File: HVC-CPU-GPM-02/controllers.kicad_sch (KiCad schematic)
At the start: 31 parts, among them P2 EXPANSION, P4 CONTROLLER 1, P5 CONTROLLER 2, U7 74LS368, U8 74LS368

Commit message: annotate schematics, correct PCB/schematic parity issure, add datasheets
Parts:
- C11, C12, C13, C14, C15, C16, C17, C18, C19, C20, C21, C22, C23, C24, C25, C26, C27, C28, C29, C30, C31, C32, C33, C9: footprint Nintendo:C_Disc_D3.0mm_W2.0mm_P3.0mm -> Nintendo:C_Disc_NoSilk_D3.0mm_W2.0mm_P3.0mm
- R8: footprint Resistor_THT:R_Axial_DIN0207_L6.3mm_D2.5mm_P10.16mm_Horizontal -> Nintendo:R_Axial_NoSilk_DIN0207_L6.3mm_D2.5mm_P10.16mm_Horizontal
- RM1: footprint Resistor_THT:R_Array_SIP12 -> Nintendo:R_Array_SIP12
- U7, U8: footprint Package_DIP:DIP-16_W7.62mm -> Nintendo:DIP-16_W7.62mm
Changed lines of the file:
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@@
 			)
 		)
-		(property "Footprint" "Nintendo:C_Disc_D3.0mm_W2.0mm_P3.0mm"
+		(property "Footprint" "Nintendo:C_Disc_NoSilk_D3.0mm_W2.0mm_P3.0mm"
 			(at 77.7748 90.17 0)
 			(effects
@@
 			)
 		)
-		(property "Footprint" "Nintendo:C_Disc_D3.0mm_W2.0mm_P3.0mm"
+		(property "Footprint" "Nintendo:C_Disc_NoSilk_D3.0mm_W2.0mm_P3.0mm"
 			(at 82.8548 46.99 0)
 			(effects
@@
 			)
 		)
-		(property "Footprint" "Nintendo:C_Disc_D3.0mm_W2.0mm_P3.0mm"
+		(property "Footprint" "Nintendo:C_Disc_NoSilk_D3.0mm_W2.0mm_P3.0mm"
 			(at 101.2952 153.67 0)
 			(effects
@@
 			)
 		)
-		(property "Footprint" "Resistor_THT:R_Array_SIP12"
+		(property "Footprint" "Nintendo:R_Array_SIP12"
 			(at 141.478 99.06 90)
 			(effects
@@
 			)
 		)
-		(property "Footprint" "Nintendo:C_Disc_D3.0mm_W2.0mm_P3.0mm"
+		(property "Footprint" "Nintendo:C_Disc_NoSilk_D3.0mm_W2.0mm_P3.0mm"
 			(at 82.8548 90.17 0)
 			(effects
@@
 			)
 		)
-		(property "Footprint" "Resistor_THT:R_Array_SIP12"
+		(property "Footprint" "Nintendo:R_Array_SIP12"
 			(at 182.118 99.06 90)
 			(effects
@@
 			)
 		)
-		(property "Footprint" "Nintendo:C_Disc_D3.0mm_W2.0mm_P3.0mm"
+		(property "Footprint" "Nintendo:C_Disc_NoSilk_D3.0mm_W2.0mm_P3.0mm"
 			(at 91.1352 153.67 0)
 			(effects
@@
 			)
 		)
-		(property "Footprint" "Package_DIP:DIP-16_W7.62mm"
+		(property "Footprint" "Nintendo:DIP-16_W7.62mm"
 			(at 227.33 147.32 0)
 			(effects
@@
 			)
 		)
-		(property "Datasheet" "http://www.ti.com/lit/gpn/sn74LS368"
+		(property "Datasheet" "kicad-embed://74LS368.pdf"
 			(at 227.33 147.32 0)
 			(effects
@@
 			)
 		)
-		(property "Footprint" "Nintendo:C_Disc_D3.0mm_W2.0mm_P3.0mm"
+		(property "Footprint" "Nintendo:C_Disc_NoSilk_D3.0mm_W2.0mm_P3.0mm"
 			(at 70.8152 153.67 0)
 			(effects
@@
 			)
 		)
-		(property "Footprint" "Resistor_THT:R_Array_SIP12"
+		(property "Footprint" "Nintendo:R_Array_SIP12"
 			(at 168.148 26.67 90)
 			(effects
@@
 			)
 		)
-		(property "Footprint" "Resistor_THT:R_Array_SIP12"
+		(property "Footprint" "Nintendo:R_Array_SIP12"
 			(at 182.372 26.67 90)
 			(effects
@@
 			)
 		)
-		(property "Footprint" "Nintendo:C_Disc_D3.0mm_W2.0mm_P3.0mm"
+		(property "Footprint" "Nintendo:C_Disc_NoSilk_D3.0mm_W2.0mm_P3.0mm"
 			(at 191.4652 63.5 0)
 			(effects
@@
 			)
 		)
-		(property "Footprint" "Resistor_THT:R_Array_SIP12"
+		(property "Footprint" "Nintendo:R_Array_SIP12"
 			(at 157.988 26.67 90)
 			(effects
@@
 			)
 		)
-		(property "Footprint" "Nintendo:C_Disc_D3.0mm_W2.0mm_P3.0mm"
+		(property "Footprint" "Nintendo:C_Disc_NoSilk_D3.0mm_W2.0mm_P3.0mm"
 			(at 50.4952 153.67 0)
 			(effects
@@
 			)
 		)
-		(property "Footprint" "Nintendo:C_Disc_D3.0mm_W2.0mm_P3.0mm"
+		(property "Footprint" "Nintendo:C_Disc_NoSilk_D3.0mm_W2.0mm_P3.0mm"
 			(at 80.9752 153.67 0)
 			(effects
@@
 			)
 		)
-		(property "Footprint" "Resistor_THT:R_Array_SIP12"
+		(property "Footprint" "Nintendo:R_Array_SIP12"
 			(at 151.638 99.06 90)
 			(effects
@@
 			)
 		)
-		(property "Footprint" "Nintendo:C_Disc_D3.0mm_W2.0mm_P3.0mm"
+		(property "Footprint" "Nintendo:C_Disc_NoSilk_D3.0mm_W2.0mm_P3.0mm"
 			(at 116.5352 153.67 0)
 			(effects
@@
 			)
 		)
-		(property "Footprint" "Nintendo:C_Disc_D3.0mm_W2.0mm_P3.0mm"
+		(property "Footprint" "Nintendo:C_Disc_NoSilk_D3.0mm_W2.0mm_P3.0mm"
 			(at 75.8952 153.67 0)
 			(effects
@@
 			)
 		)
-		(property "Footprint" "Nintendo:C_Disc_D3.0mm_W2.0mm_P3.0mm"
+		(property "Footprint" "Nintendo:C_Disc_NoSilk_D3.0mm_W2.0mm_P3.0mm"
 			(at 98.0948 46.99 0)
 			(effects
@@
 			)
 		)
-		(property "Footprint" "Package_DIP:DIP-16_W7.62mm"
+		(property "Footprint" "Nintendo:DIP-16_W7.62mm"
 			(at 227.33 128.27 0)
 			(effects
@@
 			)
 		)
-		(property "Datasheet" "http://www.ti.com/lit/gpn/sn74LS368"
+		(property "Datasheet" "kicad-embed://74LS368.pdf"
 			(at 227.33 128.27 0)
 			(effects
@@
 			)
 		)
-		(property "Footprint" "Resistor_THT:R_Array_SIP12"
+		(property "Footprint" "Nintendo:R_Array_SIP12"
 			(at 161.798 99.06 90)
 			(effects
@@
 			)
 		)
-		(property "Footprint" "Package_DIP:DIP-16_W7.62mm"
+		(property "Footprint" "Nintendo:DIP-16_W7.62mm"
 			(at 227.33 45.72 0)
 			(effects
@@
 			)
 		)
-		(property "Datasheet" "http://www.ti.com/lit/gpn/sn74LS368"
+		(property "Datasheet" "kicad-embed://74LS368.pdf"
 			(at 227.33 45.72 0)
 			(effects
@@
 			)
 		)
-		(property "Footprint" "Nintendo:C_Disc_D3.0mm_W2.0mm_P3.0mm"
+		(property "Footprint" "Nintendo:C_Disc_NoSilk_D3.0mm_W2.0mm_P3.0mm"
 			(at 96.2152 153.67 0)
 			(effects
@@
 			)
 		)
-		(property "Footprint" "Nintendo:C_Disc_D3.0mm_W2.0mm_P3.0mm"
+		(property "Footprint" "Nintendo:C_Disc_NoSilk_D3.0mm_W2.0mm_P3.0mm"
 			(at 87.9348 46.99 0)
 			(effects
@@
 			)
 		)
-		(property "Footprint" "Nintendo:C_Disc_D3.0mm_W2.0mm_P3.0mm"
+		(property "Footprint" "Nintendo:C_Disc_NoSilk_D3.0mm_W2.0mm_P3.0mm"
 			(at 86.0552 153.67 0)
 			(effects
@@
 			)
 		)
-		(property "Footprint" "Resistor_THT:R_Array_SIP12"
+		(property "Footprint" "Nintendo:R_Array_SIP12"
 			(at 171.958 99.06 90)
 			(effects
@@
 			)
 		)
-		(property "Footprint" "Nintendo:C_Disc_D3.0mm_W2.0mm_P3.0mm"
+		(property "Footprint" "Nintendo:C_Disc_NoSilk_D3.0mm_W2.0mm_P3.0mm"
 			(at 87.9348 90.17 0)
 			(effects
@@
 			)
 		)
-		(property "Footprint" "Nintendo:C_Disc_D3.0mm_W2.0mm_P3.0mm"
+		(property "Footprint" "Nintendo:C_Disc_NoSilk_D3.0mm_W2.0mm_P3.0mm"
 			(at 106.3752 153.67 0)
 			(effects
@@
 			)
 		)
-		(property "Footprint" "Nintendo:C_Disc_D3.0mm_W2.0mm_P3.0mm"
+		(property "Footprint" "Nintendo:C_Disc_NoSilk_D3.0mm_W2.0mm_P3.0mm"
 			(at 55.5752 153.67 0)
 			(effects
@@
 			)
 		)
-		(property "Footprint" "Resistor_THT:R_Array_SIP12"
+		(property "Footprint" "Nintendo:R_Array_SIP12"
 			(at 192.278 99.06 90)
 			(effects
@@
 			)
 		)
-		(property "Footprint" "Nintendo:C_Disc_D3.0mm_W2.0mm_P3.0mm"
+		(property "Footprint" "Nintendo:C_Disc_NoSilk_D3.0mm_W2.0mm_P3.0mm"
 			(at 93.0148 46.99 0)
 			(effects
@@
 			)
 		)
-		(property "Footprint" "Nintendo:C_Disc_D3.0mm_W2.0mm_P3.0mm"
+		(property "Footprint" "Nintendo:C_Disc_NoSilk_D3.0mm_W2.0mm_P3.0mm"
 			(at 111.4552 153.67 0)
 			(effects
@@
 			)
 		)
-		(property "Footprint" "Nintendo:C_Disc_D3.0mm_W2.0mm_P3.0mm"
+		(property "Footprint" "Nintendo:C_Disc_NoSilk_D3.0mm_W2.0mm_P3.0mm"
 			(at 93.0148 90.17 0)
 			(effects
@@
 			)
 		)
-		(property "Footprint" "Nintendo:C_Disc_D3.0mm_W2.0mm_P3.0mm"
+		(property "Footprint" "Nintendo:C_Disc_NoSilk_D3.0mm_W2.0mm_P3.0mm"
 			(at 60.6552 153.67 0)
 			(effects
@@
 			)
 		)
-		(property "Footprint" "Nintendo:C_Disc_D3.0mm_W2.0mm_P3.0mm"
+		(property "Footprint" "Nintendo:C_Disc_NoSilk_D3.0mm_W2.0mm_P3.0mm"
 			(at 98.0948 90.17 0)
 			(effects
@@
 			)
 		)
-		(property "Footprint" "Nintendo:C_Disc_D3.0mm_W2.0mm_P3.0mm"
+		(property "Footprint" "Nintendo:C_Disc_NoSilk_D3.0mm_W2.0mm_P3.0mm"
 			(at 65.7352 153.67 0)
 			(effects
@@
 			)
 		)
-		(property "Footprint" "Resistor_THT:R_Axial_DIN0207_L6.3mm_D2.5mm_P10.16mm_Horizontal"
+		(property "Footprint" "Nintendo:R_Axial_NoSilk_DIN0207_L6.3mm_D2.5mm_P10.16mm_Horizontal"
 			(at 181.61 55.118 90)
 			(effects

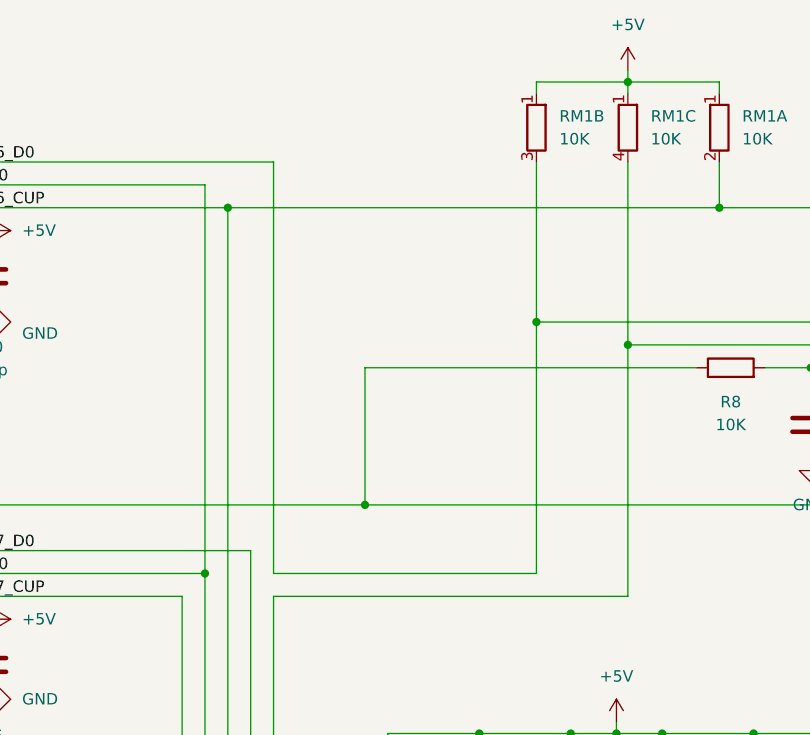
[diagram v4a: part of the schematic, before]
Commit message: Updated PCB and footprints to correct hole and pad sizes
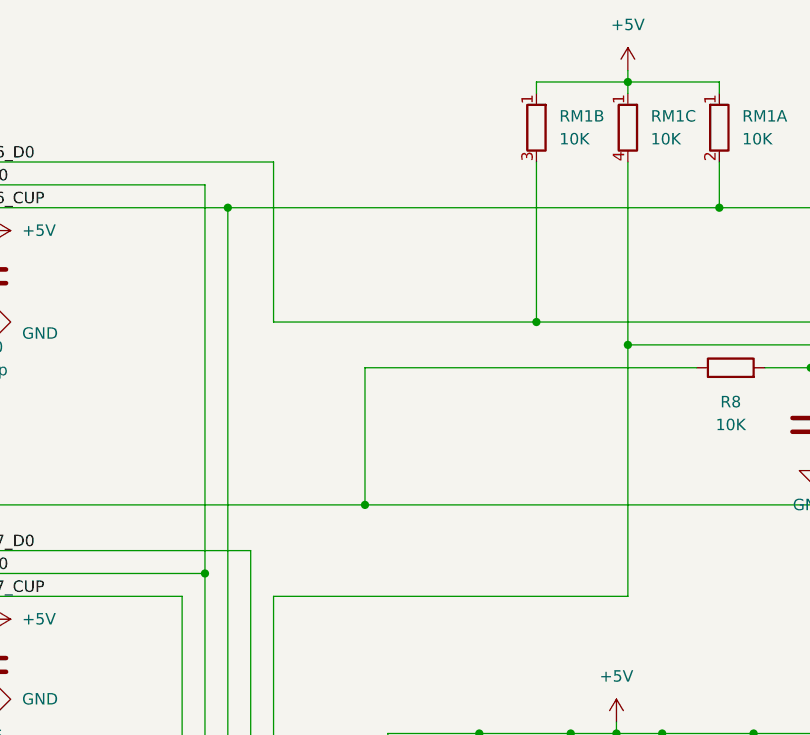
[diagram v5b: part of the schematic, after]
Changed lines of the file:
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@@
 	(wire
 		(pts
-			(xy 130.81 76.2) (xy 160.02 76.2)
+			(xy 130.81 48.26) (xy 160.02 48.26)
 		)
 		(stroke
@@
 	(wire
 		(pts
-			(xy 160.02 48.26) (xy 160.02 76.2)
-		)
-		(stroke
-			(width 0)
-			(type default)
-		)
-	)
-	(wire
-		(pts
 			(xy 262.89 135.89) (xy 262.89 86.36)
 		)
@@
 	(wire
 		(pts
-			(xy 130.81 30.48) (xy 130.81 76.2)
-		)
-		(stroke
+			(xy 130.81 30.48) (xy 130.81 48.26)
+		)
+		(stroke
